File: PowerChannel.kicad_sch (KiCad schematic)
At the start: 15 parts, among them J3 Screw_Terminal_01x04, Q1 2N7002, Q2 NTF6P02, Q3 2N7002, U2 INA219xID

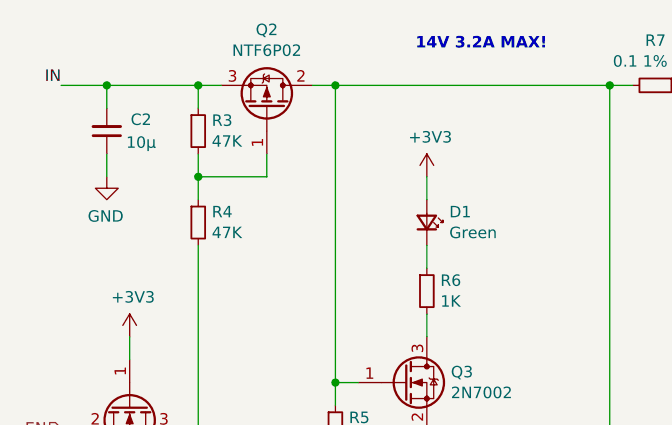
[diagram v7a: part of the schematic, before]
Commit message: Replace NTF6P02 by DMP6023LE-13
This requires updating the voltage divider providing gate voltage for
the larger Gate Threshold (and Gate-Source) Voltage.

Signed-off-by: Geert Uytterhoeven <geert@linux-m68k.org>
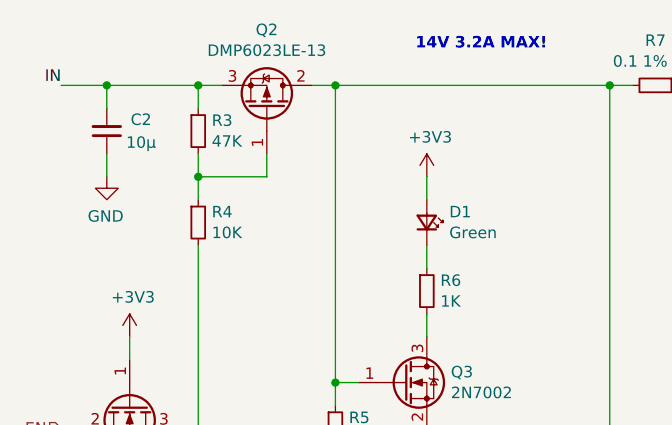
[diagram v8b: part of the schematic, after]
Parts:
- Q2: value NTF6P02 -> DMP6023LE-13
- R4: value 47K -> 10K
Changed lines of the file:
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@@
       (effects (font (size 1.27 1.27)) (justify left))
     )
-    (property "Value" "47K" (id 1) (at 54.8386 41.783 0)
+    (property "Value" "10K" (id 1) (at 54.8386 41.783 0)
       (effects (font (size 1.27 1.27)) (justify left))
     )
@@
     (in_bom yes) (on_board yes)
     (property "Reference" "Q2" (id 0) (at 60.96 19.2278 90))
-    (property "Value" "NTF6P02" (id 1) (at 60.96 21.5392 90))
+    (property "Value" "DMP6023LE-13" (id 1) (at 60.96 21.5392 90))
     (property "Footprint" "Package_TO_SOT_SMD:SOT-223-3_TabPin2" (id 2) (at 59.055 22.86 0)
       (effects (font (size 1.27 1.27) italic) (justify left) hide)
     )
-    (property "Datasheet" "http://www.irf.com/product-info/datasheets/data/irf9540n.pdf" (id 3) (at 60.96 27.94 0)
+    (property "Datasheet" "https://www.diodes.com/assets/Datasheets/DMP6023LE.pdf" (id 3) (at 60.96 27.94 0)
       (effects (font (size 1.27 1.27)) (justify left) hide)
     )
